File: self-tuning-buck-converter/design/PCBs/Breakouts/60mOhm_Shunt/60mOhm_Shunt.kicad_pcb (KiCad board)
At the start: 2 copper layers, 15.2 x 7.6 mm, 5 parts, among them J1 Input +, J2 Kelvin +, J3 Input -, J4 Kelvin -

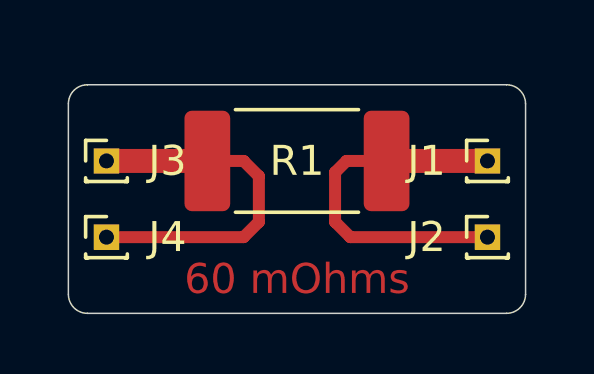
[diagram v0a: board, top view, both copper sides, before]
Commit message: update breakout PCB's for the 50mO and 60mO resistors. Ordered the missing parts
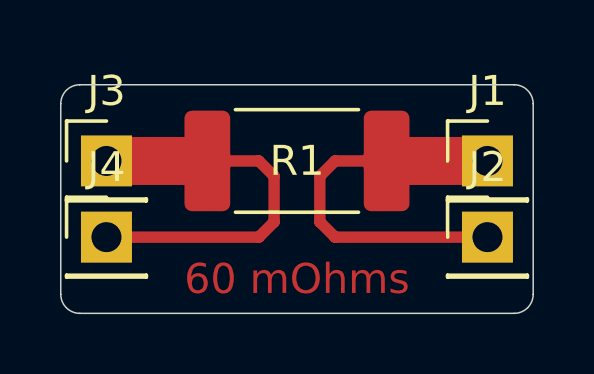
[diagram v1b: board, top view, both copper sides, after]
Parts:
- J1, J2, J3, J4: footprint Connector_PinHeader_1.00mm:PinHeader_1x01_P1.00mm_Vertical -> Connector_PinHeader_2.54mm:PinHeader_1x01_P2.54mm_Vertical
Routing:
- net Net-(J3-Pad1): track 12.1 -> 13.1 mm
- net Net-(J1-Pad1): track 12.2 -> 13.1 mm
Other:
- board size 15.2 x 7.6 mm -> 15.7 x 7.6 mm
- net class Default: clearance 0.2 -> 0.381; trace_width 0.25 -> 0.381
- rule trace_clearance: 0.2 -> 0.381
- rule trace_min: 0.2 -> 0.381

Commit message: updated breakout PCB's
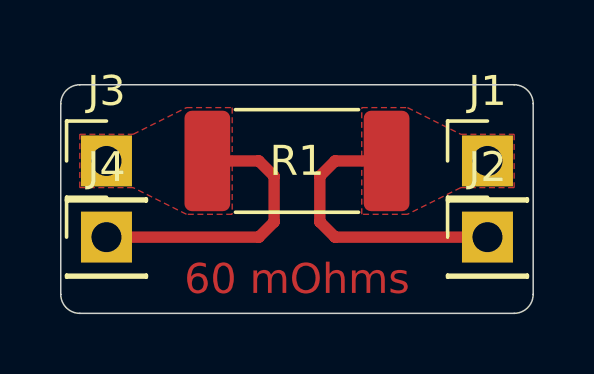
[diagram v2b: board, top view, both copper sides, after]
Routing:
- net Net-(J3-Pad1): track 13.1 -> 9.76 mm
- net Net-(J1-Pad1): track 13.1 -> 9.76 mm
- added copper zone on F.Cu, net Net-(J1-Pad1)
- added copper zone on F.Cu, net Net-(J3-Pad1)
